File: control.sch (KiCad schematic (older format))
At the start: 50 parts, among them J401 CHG, J402 CTRL, J403 SOICbite, J404 RS485, SW401 RESET, SW402 USER, U401 STM32F072CBTx, U402 CH340G, U403 SP3485EN, Y401 12MHz, Y402 12MHz

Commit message: finished routing. no silk artwork.
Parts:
- renumbered C413 to C401, C414 to C402, C401 to C403, C402 to C404, C403 to C405, C404 to C406, C405 to C407, C406 to C408, C407 to C409, C408 to C410, C409 to C411, C410 to C412, C411 to C413, C412 to C414, J402 to J401, J401 to J402, NT402 to NT401, NT403 to NT402, NT401 to NT403, R403 to R401, R401 to R402, R402 to R403, R411 to R407, R410 to R408, R412 to R409, R413 to R410, SW402 to SW401, SW401 to SW402, Y402 to Y401, Y401 to Y402

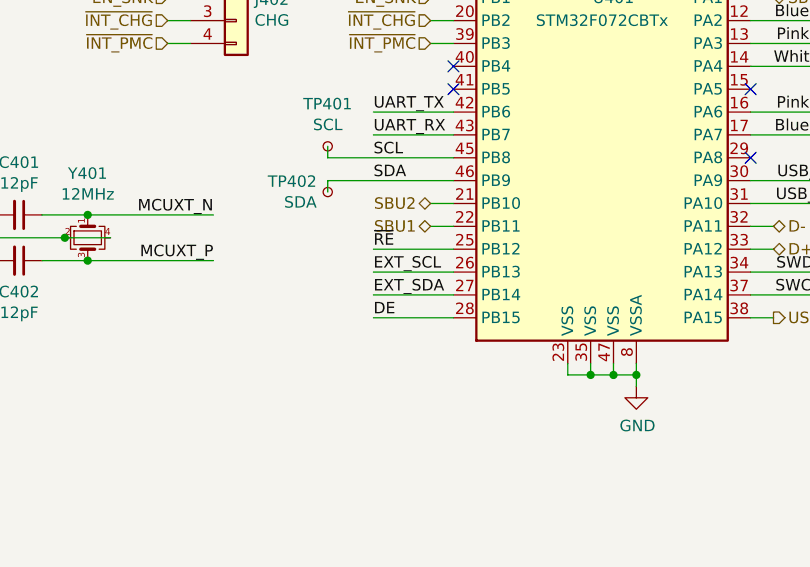
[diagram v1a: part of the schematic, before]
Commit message: Add a few more parts, fix PCB origin problem
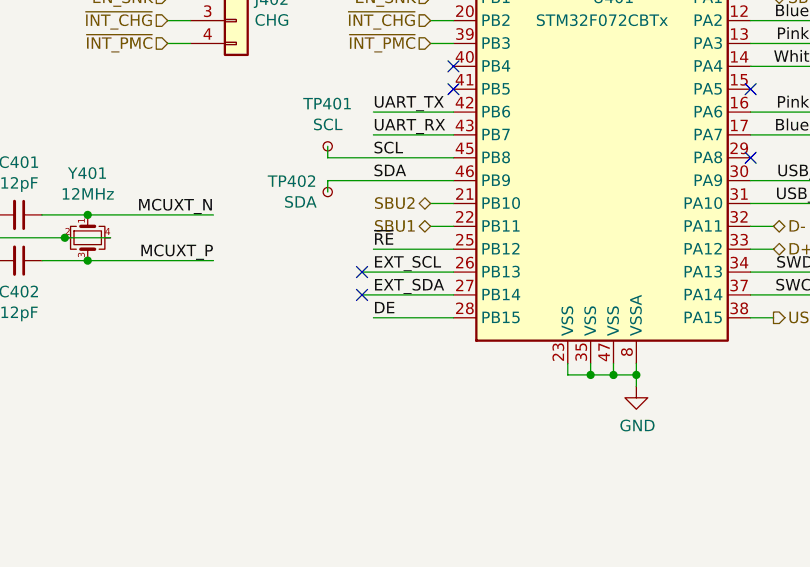
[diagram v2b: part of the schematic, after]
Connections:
- no-connect marks 20 -> 22
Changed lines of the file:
@@
 Text Label 2900 4200 0    50   ~ 0
 EXT_SDA
-Wire Wire Line
-	2900 4100 3250 4100
-Wire Wire Line
-	3250 4200 2900 4200
 NoConn ~ 4550 3300
 NoConn ~ 4550 3600
@@
 Text Label 2200 3850 2    50   ~ 0
 MCUXT_N
+Wire Wire Line
+	2850 4100 3250 4100
+Wire Wire Line
+	2850 4200 3250 4200
+NoConn ~ 2850 4100
+NoConn ~ 2850 4200
 $EndSCHEMATC

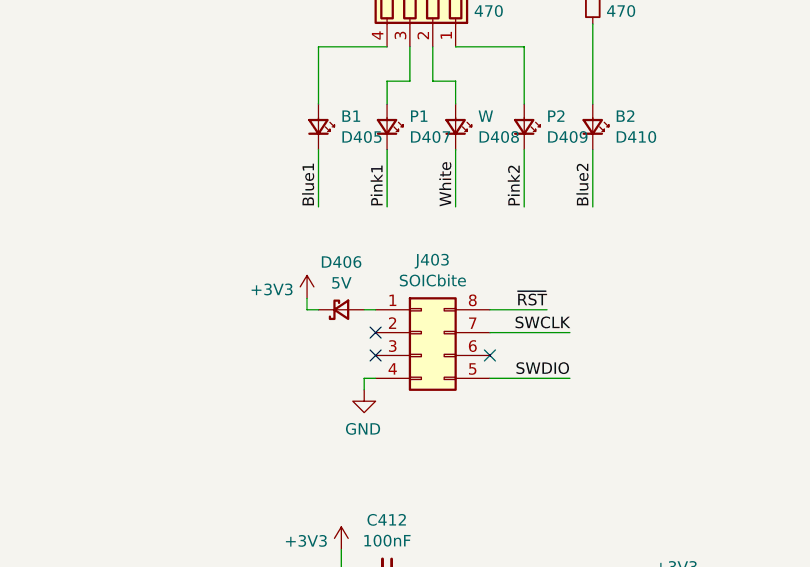
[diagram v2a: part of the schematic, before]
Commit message: added missing JLC/LCSC parts
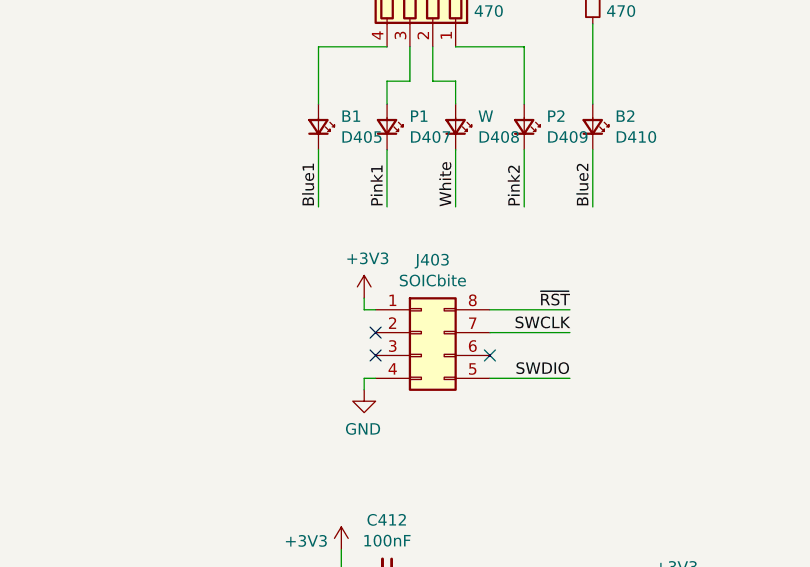
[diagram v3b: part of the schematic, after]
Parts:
- removed D406: 5V, Diode_SMD:D_SOD-123, symbol Device:D_Schottky_Small
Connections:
- net +3V3: now also J403.1 (Pin_1)
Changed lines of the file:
@@
 L power:+3V3 #PWR0419
 U 1 1 5F0F5EDC
-P 7950 4050
-F 0 "#PWR0419" H 7950 3900 50  0001 C CNN
-F 1 "+3V3" H 7892 4087 50  0000 R CNN
-F 2 "" H 7950 4050 50  0001 C CNN
-F 3 "" H 7950 4050 50  0001 C CNN
-	1    7950 4050
-	1    0    0    -1
-$EndComp
-$Comp
-L Device:D_Schottky_Small D406
-U 1 1 5F0FC49F
-P 8100 4100
-F 0 "D406" H 8100 3893 50  0000 C CNN
-F 1 "5V" H 8100 3984 50  0000 C CNN
-F 2 "Diode_SMD:D_SOD-123" V 8100 4100 50  0001 C CNN
-F 3 "~" V 8100 4100 50  0001 C CNN
-	1    8100 4100
-	1    0    0    1
-$EndComp
-Wire Wire Line
-	7950 4050 7950 4100
-Wire Wire Line
-	8000 4100 7950 4100
-Wire Wire Line
-	8250 4100 8200 4100
-Text Label 9000 4100 2    50   ~ 0
+P 8200 4050
+F 0 "#PWR0419" H 8200 3900 50  0001 C CNN
+F 1 "+3V3" H 8215 4223 50  0000 C CNN
+F 2 "" H 8200 4050 50  0001 C CNN
+F 3 "" H 8200 4050 50  0001 C CNN
+	1    8200 4050
+	1    0    0    -1
+$EndComp
+Wire Wire Line
+	8200 4050 8200 4100
+Text Label 9100 4100 2    50   ~ 0
 ~RST
 Wire Wire Line
-	9000 4100 8750 4100
+	9100 4100 8750 4100
 Text Label 9100 4400 2    50   ~ 0
 SWDIO
@@
 NoConn ~ 2850 4100
 NoConn ~ 2850 4200
+Wire Wire Line
+	8200 4100 8250 4100
 $EndSCHEMATC

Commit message: It's production ready now. Bottom half is fully assembled by JLC.
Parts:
- D403, D404: JLC (none) -> SOD-523; LCSC (none) -> C61148; MPN (none) -> ESD5Z3.3T1G
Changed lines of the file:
@@
 F 1 "5V" V 3345 6421 50  0000 R CNN
 F 2 "Diode_SMD:D_SOD-523" H 3300 6500 50  0001 C CNN
-F 3 "~" H 3300 6500 50  0001 C CNN
+F 3 "https://datasheet.lcsc.com/szlcsc/ON-Semicon-ON-ESD5Z3-3T1G_C61148.pdf" H 3300 6500 50  0001 C CNN
+F 4 "SOD-523" H 3300 6500 50  0001 C CNN "JLC"
+F 5 "C61148" H 3300 6500 50  0001 C CNN "LCSC"
+F 6 "ESD5Z3.3T1G" H 3300 6500 50  0001 C CNN "MPN"
 	1    3300 6500
 	0    -1   1    0
@@
 F 1 "5V" V 2945 6621 50  0000 R CNN
 F 2 "Diode_SMD:D_SOD-523" H 2900 6700 50  0001 C CNN
-F 3 "~" H 2900 6700 50  0001 C CNN
+F 3 "https://datasheet.lcsc.com/szlcsc/ON-Semicon-ON-ESD5Z3-3T1G_C61148.pdf" H 2900 6700 50  0001 C CNN
+F 4 "SOD-523" H 2900 6700 50  0001 C CNN "JLC"
+F 5 "C61148" H 2900 6700 50  0001 C CNN "LCSC"
+F 6 "ESD5Z3.3T1G" H 2900 6700 50  0001 C CNN "MPN"
 	1    2900 6700
 	0    -1   1    0

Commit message: added 3D models
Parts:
- J401: footprint Connector_USB:USB_C_Receptacle_XKB_U262-16XN-4BVC11 -> Automated:USB_C_Receptacle_XKB_U262-16XN-4BVC11
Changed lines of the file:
@@
 F 0 "J401" H 1420 6289 50  0000 R CNN
 F 1 "CTRL" H 1420 6198 50  0000 R CNN
-F 2 "Connector_USB:USB_C_Receptacle_XKB_U262-16XN-4BVC11" H 2000 6350 50  0001 C CNN
+F 2 "Automated:USB_C_Receptacle_XKB_U262-16XN-4BVC11" H 2000 6350 50  0001 C CNN
 F 3 "https://www.usb.org/sites/default/files/documents/usb_type-c.zip" H 2000 6350 50  0001 C CNN
 	1    1850 6350
